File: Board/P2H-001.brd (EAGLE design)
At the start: 94.9 x 72.4 mm, 29 parts, among them IC1 74LS157N, IC2 LTC485N, IC3 74LS07N, IC4 LTC485N, IC5 4066N, IC6 TLC5941NT, IC7 TLC5941NT

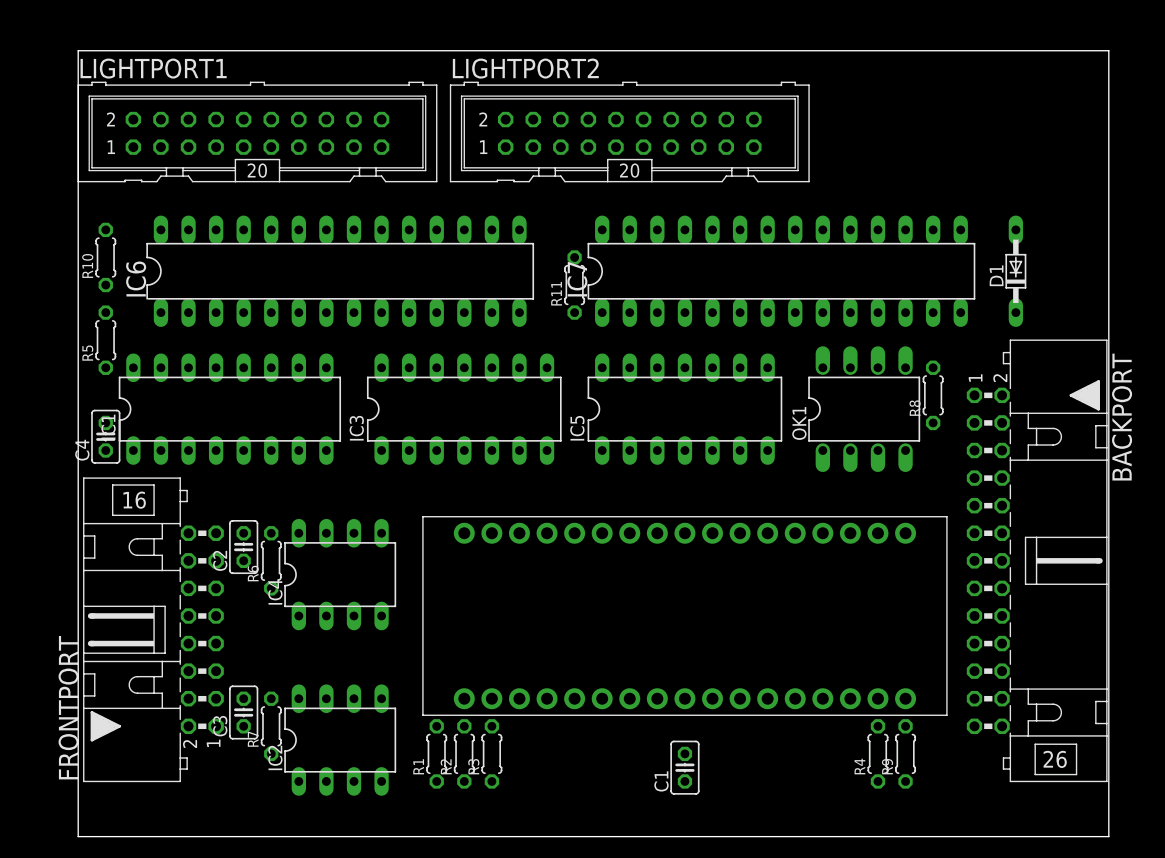
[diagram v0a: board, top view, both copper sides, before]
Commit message: Redesigned for ICB-93 size.
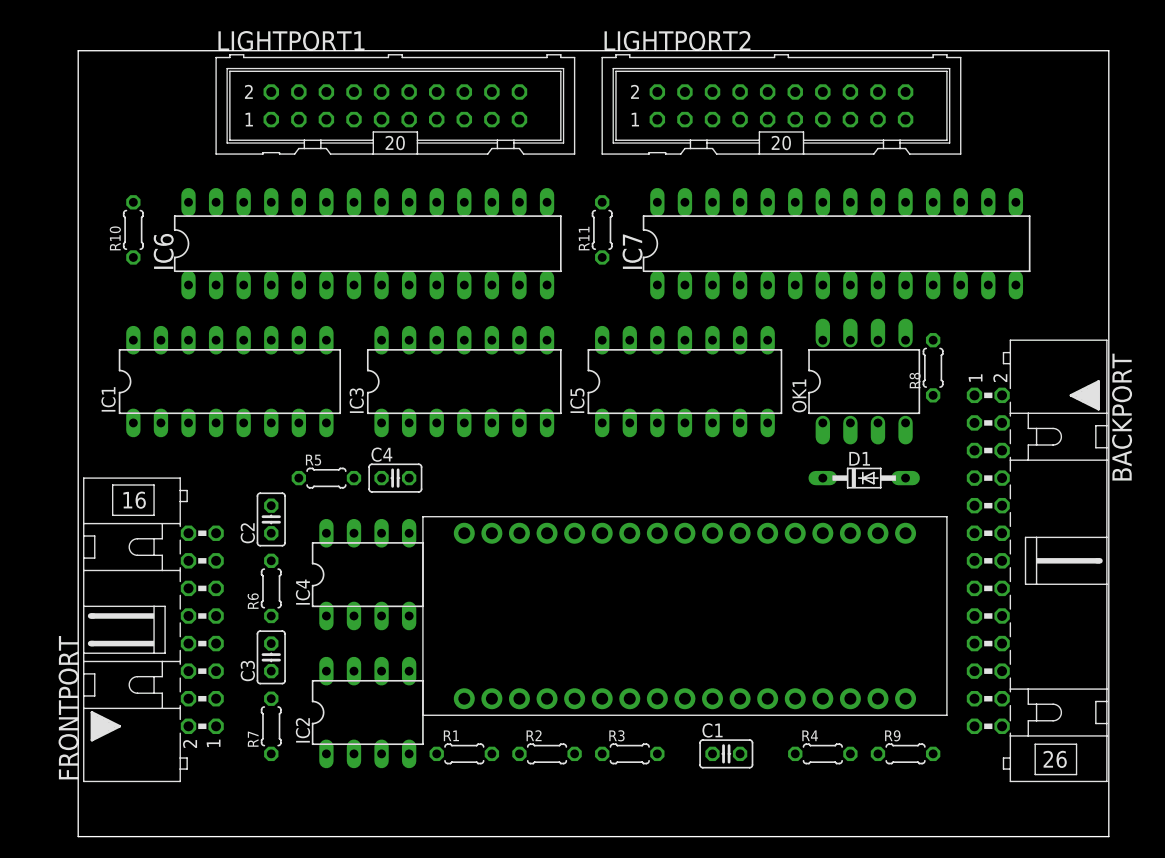
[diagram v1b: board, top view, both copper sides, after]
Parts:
- moved C4 26.9 mm to (29.2, 33.0), turned to 0 degrees
- moved R5 24.0 mm to (22.9, 33.0), turned to 0 degrees
- moved D1 23.6 mm to (72.4, 33.0), turned to 0 degrees
- moved LIGHTPORT2 14.2 mm to (64.8, 67.3)
- moved LIGHTPORT1 13.0 mm to (29.2, 67.3)
- moved R3 12.7 mm to (50.8, 7.62), turned to 0 degrees
- moved R2 7.62 mm to (43.2, 7.62), turned to 0 degrees
- moved R11 5.68 mm to (48.3, 55.9)
- moved C3 5.68 mm to (17.8, 16.5)
- moved IC7 5.68 mm to (69.8, 54.6)
- moved R4 5.08 mm to (68.6, 7.62), turned to 0 degrees
- moved C1 4.02 mm to (59.7, 7.62), turned to 0 degrees
- moved IC2 3.59 mm to (26.7, 11.4)
- moved IC6 3.59 mm to (26.7, 54.6)
- moved C2 3.59 mm to (17.8, 29.2)
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
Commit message: Design renewed.
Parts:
- removed IC7: TLC5941NT, adafruit:DIL28-3
- removed LIGHTPORT1, LIGHTPORT2: (no value), con-ml:ML20
- removed MC1: ARDUINOMICRO, adafruit:ARDUINOMICRO
- removed R10, R11: 4.7k, resistor:0204/5
- removed R9: 220, resistor:0204/5
- added C5, C6, C7: (no value), rcl:C025-025X050
- added JP1, JP2: (no value), pinhead:1X02
- added LIGHTPORT: (no value), con-ml:ML20L
- added U$1: ARDUINO_PRO_MINI, SparkFun-Boards:ARDUINO_PRO_MINI
- IC5: value 4066N -> TLC5941NT; device 40xx:DIL14 -> adafruit:DIL28-3
- R1, R2: value 330 -> 220
- R3: value 330 -> 120
- R4: value 220 -> 120
- R5: value 10k -> 220
- R6: value 120 -> 220
- R7: value 120 -> 4.7k
- R8: value 220 -> 4.7k
- moved IC2 66.7 mm to (69.8, 62.2)
- moved R3 56.8 mm to (61.0, 63.5), turned to 90 degrees
- moved R7 55.7 mm to (58.4, 48.3)
- moved IC1 51.8 mm to (64.8, 31.8)
- moved C2 51.1 mm to (59.7, 58.4), turned to 0 degrees
- moved C3 49.7 mm to (59.7, 43.2), turned to 0 degrees
- moved IC4 48.9 mm to (69.8, 47.0)
- moved R4 41.3 mm to (61.0, 48.3), turned to 90 degrees
- moved R6 35.7 mm to (53.3, 20.3)
- moved R5 35.4 mm to (55.9, 20.3), turned to 90 degrees
- moved OK1 29.7 mm to (44.5, 31.8)
- moved R8 28.7 mm to (58.4, 63.5)
- moved R1 28.4 mm to (61.0, 20.3), turned to 90 degrees
- moved D1 21.6 mm to (50.8, 31.8), turned to 90 degrees
- moved R2 19.8 mm to (58.4, 20.3), turned to 90 degrees
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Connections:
- removed net 3V3: FRONTPORT.3, MC1.P$33
- removed net GPDETECT: BACKPORT.8, MC1.P$7
- removed net LEDMAX: FRONTPORT.13, R1.1
- removed net LEDMIN: FRONTPORT.11, R3.1
- removed net N$44: IC7.5, LIGHTPORT2.10
- removed net N$45: IC7.7, LIGHTPORT2.12
- removed net N$46: IC7.9, LIGHTPORT2.14
- removed net N$47: IC7.11, LIGHTPORT2.16
- removed net N$48: IC7.13, LIGHTPORT2.18
- removed net N$49: IC7.15, LIGHTPORT2.20
- removed net N$50: IC7.2, LIGHTPORT2.7
- removed net N$51: IC7.4, LIGHTPORT2.9
- removed net N$52: IC7.6, LIGHTPORT2.11
- removed net N$53: IC7.8, LIGHTPORT2.13
- removed net N$54: IC7.10, LIGHTPORT2.15
- removed net N$55: IC7.12, LIGHTPORT2.17
- removed net N$56: IC7.14, LIGHTPORT2.19
- removed net N$57: IC6.28, LIGHTPORT1.5
- removed net N$65: IC6.15, LIGHTPORT1.20
- removed net N$66: IC6.2, LIGHTPORT1.7
- removed net N$67: IC6.4, LIGHTPORT1.9
- removed net N$68: IC6.6, LIGHTPORT1.11
- removed net N$69: IC6.8, LIGHTPORT1.13
- removed net N$70: IC6.10, LIGHTPORT1.15
- removed net N$71: IC6.12, LIGHTPORT1.17
- removed net N$72: IC6.14, LIGHTPORT1.19
- removed net N$73: IC6.11, LIGHTPORT1.16
- removed net N$74: IC6.7, LIGHTPORT1.12
- removed net N$75: IC6.9, LIGHTPORT1.14
- removed net N$76: IC6.5, LIGHTPORT1.10
- removed net N$77: IC6.3, LIGHTPORT1.8
- removed net N$78: IC6.1, LIGHTPORT1.6
- removed net N$80: IC6.13, LIGHTPORT1.18
- removed net SCL: BACKPORT.15, MC1.P$10
- removed net SDA: BACKPORT.14, MC1.P$11
- removed net VR: FRONTPORT.16, MC1.P$9
- removed net VSS: IC5.7
- removed net XDETECT: BACKPORT.10, IC1.1, MC1.P$1, R5.1
- new net LED1B: FRONTPORT.10, IC5.2
- new net LED1G: FRONTPORT.9, IC5.1
- new net LED1R: FRONTPORT.8, IC5.28
- new net LED2B: FRONTPORT.13, IC5.5
- new net LED2G: FRONTPORT.12, IC5.4
- new net LED2R: FRONTPORT.11, IC5.3
- new net LED3B: FRONTPORT.16, IC5.8
- new net LED3G: FRONTPORT.15, IC5.7
- new net LED3R: FRONTPORT.14, IC5.6
- new net N$17: BACKPORT.18, U$1.13
- new net N$20: BACKPORT.26, D1.A, OK1.3
- new net N$22: BACKPORT.17, IC5.13
- new net N$23: FRONTPORT.7, U$1.A4
- new net N$24: IC5.14, LIGHTPORT.3
- new net N$25: IC5.15, LIGHTPORT.4
- new net N$26: IC6.28, LIGHTPORT.5
- new net N$27: IC6.2, LIGHTPORT.7
- new net N$28: IC6.4, LIGHTPORT.9
- new net N$29: IC6.6, LIGHTPORT.11
- new net N$30: IC6.8, LIGHTPORT.13
- new net N$31: IC6.10, LIGHTPORT.15
- new net N$32: IC6.12, LIGHTPORT.17
- new net N$33: IC6.14, LIGHTPORT.19
- new net N$34: IC6.1, LIGHTPORT.6
- new net N$35: IC6.3, LIGHTPORT.8
- new net N$36: IC6.5, LIGHTPORT.10
- new net N$40: IC6.9, LIGHTPORT.14
- new net SWRST: FRONTPORT.4, U$1.3
- new net XBAR: BACKPORT.5, IC1.1, U$1.11
- net BLANK: now also BACKPORT.4, IC5.23, U$1.7; no longer IC5.2, IC7.23
- net GND: now also C5.2, C6.2, C7.2, IC1.10, IC1.11, IC1.13, IC1.14, IC1.5, IC1.6, IC3.11, IC3.13, IC3.3, IC3.5, IC3.9, IC5.22, LIGHTPORT.2, U$1.23; no longer BACKPORT.4, FRONTPORT.10, FRONTPORT.12, FRONTPORT.14, FRONTPORT.4, FRONTPORT.6, FRONTPORT.8, IC7.22, LIGHTPORT1.2, LIGHTPORT1.4, LIGHTPORT2.2, LIGHTPORT2.4, MC1.P$12, MC1.P$21
- net GSCLCK: now also IC5.18, U$1.8; no longer BACKPORT.12, IC7.18, MC1.P$8
- net HSRX: now also IC1.3; no longer IC1.2
- net MIDIRX: now also IC1.2, JP2.2; no longer IC1.3
- net MODE: now also IC5.27, U$1.9; no longer IC5.9, IC7.27
- net N$1: now also IC1.4, JP1.2, JP2.1; no longer BACKPORT.3, MC1.P$31
- net N$10: now also BACKPORT.10, U$1.20; no longer FRONTPORT.5, MC1.P$22
- net N$11: now also BACKPORT.13, IC5.9; no longer BACKPORT.11, IC5.4, MC1.P$27
- net N$12: now also BACKPORT.14, IC5.10; no longer BACKPORT.13, IC5.8, MC1.P$26
- net N$13: now also R5.1; no longer R8.1
- net N$14: now also BACKPORT.15, IC5.11; no longer BACKPORT.19, R9.1
- net N$15: now also BACKPORT.24, R2.2; no longer BACKPORT.20, R4.2
- net N$16: now also IC5.17, IC6.26; no longer IC6.17, IC7.26
- net N$18: now also BACKPORT.25, R5.2; no longer BACKPORT.21, R8.2
- net N$19: now also BACKPORT.11, U$1.A6; no longer BACKPORT.17, MC1.P$19
- net N$2: now also R2.1; no longer R4.1
- net N$21: now also BACKPORT.16, IC5.12; no longer MC1.P$3, R1.2
- net N$3: now also BACKPORT.6, U$1.12; no longer FRONTPORT.15, R2.1
- net N$37: now also IC5.20, R7.2; no longer IC6.20, R10.2
- net N$38: now also IC6.20, R8.2; no longer IC7.20, R11.2
- net N$39: now also IC6.7, LIGHTPORT.12; no longer IC7.28, LIGHTPORT2.5
- net N$4: now also BACKPORT.23, R6.1; no longer BACKPORT.5, MC1.P$30
- net N$41: now also IC6.11, LIGHTPORT.16; no longer IC7.1, LIGHTPORT2.6
- net N$42: now also IC6.13, LIGHTPORT.18; no longer BACKPORT.22, D1.A, OK1.3
- net N$43: now also IC6.15, LIGHTPORT.20; no longer IC7.3, LIGHTPORT2.8
- net N$5: now also BACKPORT.12, U$1.A7; no longer MC1.P$4, R3.2
- net N$6: now also U$1.17; no longer MC1.P$29
- net N$7: now also FRONTPORT.3, R1.1; no longer MC1.P$34, R2.2
- net N$8: now also BACKPORT.8, U$1.18; no longer IC5.13, IC5.5, IC5.6, MC1.P$2
- net N$9: now also U$1.19; no longer IC5.1, MC1.P$28
- net RX: now also JP1.1, U$1.2; no longer IC1.4, MC1.P$14
- net RX+: now also BACKPORT.19, R4.1; no longer BACKPORT.23, R7.1
- net RX-: now also BACKPORT.20, R4.2; no longer BACKPORT.24, R7.2
- net SCLCK: now also IC5.25, U$1.16; no longer BACKPORT.18, IC7.25, MC1.P$18
- net SIN: now also IC5.26, U$1.14; no longer BACKPORT.16, IC6.26, MC1.P$17
- net SWMAX: now also FRONTPORT.6, U$1.6; no longer FRONTPORT.9, MC1.P$5
- net SWMIN: now also FRONTPORT.5, U$1.5; no longer FRONTPORT.7, MC1.P$6
- net TX: now also U$1.1; no longer MC1.P$15
- net TX+: now also BACKPORT.21, R3.1; no longer BACKPORT.25, R6.1
- net TX-: now also BACKPORT.22, R3.2; no longer BACKPORT.26, R6.2
- net VCC: now also BACKPORT.1, C5.1, C6.1, C7.1, IC5.19, IC5.21, R6.2, R7.1, R8.1, U$1.21; no longer BACKPORT.6, IC7.19, IC7.21, MC1.P$23, R10.1, R11.1, R5.2, R9.2
- net VDD: now also BACKPORT.3, LIGHTPORT.1, R1.2, U$1.24; no longer BACKPORT.1, IC5.14, LIGHTPORT1.1, LIGHTPORT1.3, LIGHTPORT2.1, LIGHTPORT2.3, MC1.P$20
- net XLAT: now also IC5.24, U$1.10; no longer IC5.3, IC7.24

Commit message: Slightly re-arranged.
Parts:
- moved BACKPORT 10.2 mm to (82.5, 35.6)
- moved D1 2.54 mm to (53.3, 31.8)
- moved IC1 2.54 mm to (67.3, 31.8)
- moved IC2 2.54 mm to (72.4, 62.2)
- moved IC4 2.54 mm to (72.4, 47.0)
- moved C4 2.54 mm to (17.8, 47.0)
- moved C5 2.54 mm to (17.8, 62.2)
- moved C6 2.54 mm to (17.8, 31.8)
- moved C1 2.54 mm to (62.2, 7.62)
- moved C2 2.54 mm to (62.2, 58.4)
- moved C3 2.54 mm to (62.2, 43.2)
- moved C7 2.54 mm to (62.2, 15.2)
- moved IC3 2.54 mm to (30.5, 31.8)
- moved IC5 2.54 mm to (39.4, 47.0)
- moved IC6 2.54 mm to (39.4, 62.2)
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
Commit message: Autorouted.
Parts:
- renumbered BACKPORT to SV2, FRONTPORT to SV1, LIGHTPORT to SV3
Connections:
- net N$3 renamed GDETECT
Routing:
- net GND: track 0.00 -> 400.2 mm
- net VCC: track 0.00 -> 310.3 mm, vias 0 -> 5
- net N$8: track 0.00 -> 170.4 mm
- net BLANK: track 0.00 -> 168.5 mm, vias 0 -> 4
- net VDD: track 0.00 -> 154.4 mm, vias 0 -> 5
- net TX: track 0.00 -> 141.3 mm
- net XBAR: track 0.00 -> 122.7 mm
- net MODE: track 0.00 -> 103.7 mm, vias 0 -> 3
- net N$25: track 0.00 -> 97.6 mm, vias 0 -> 1
- net N$30: track 0.00 -> 94.8 mm, vias 0 -> 2
- net XLAT: track 0.00 -> 87.3 mm, vias 0 -> 5
- net SWRST: track 0.00 -> 86.0 mm, vias 0 -> 1
- net GSCLCK: track 0.00 -> 84.6 mm, vias 0 -> 2
- net N$9: track 0.00 -> 83.0 mm, vias 0 -> 2
- net TX+: track 0.00 -> 74.3 mm
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
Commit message: square design.
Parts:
- removed JP2: (no value), pinhead:1X02
- moved C1 54.6 mm to (62.2, 62.2), turned to 90 degrees
- moved C2 25.7 mm to (36.8, 54.6)
- moved C3 25.7 mm to (36.8, 39.4)
- moved IC1 25.4 mm to (41.9, 31.8)
- moved JP1 22.9 mm to (54.6, 31.8)
- moved SV2 19.0 mm to (63.5, 35.6)
- moved IC2 17.8 mm to (54.6, 62.2)
- moved IC4 17.8 mm to (54.6, 47.0)
- moved R7 16.6 mm to (47.0, 39.4), turned to 0 degrees
- moved R8 16.6 mm to (47.0, 54.6), turned to 0 degrees
- moved C4 13.7 mm to (29.2, 39.4), turned to 0 degrees
- moved C5 13.7 mm to (29.2, 54.6), turned to 0 degrees
- moved OK1 13.7 mm to (52.1, 19.1)
- moved R1 13.1 mm to (57.1, 8.89)
- moved R2 13.1 mm to (54.6, 8.89)
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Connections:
- net MIDIRX: no longer JP2.2
- net N$1: no longer JP2.1
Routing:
- net GND: track 400.2 -> 265.3 mm
- net N$8: track 170.4 -> 54.1 mm, vias 0 -> 2
- net SWRST: track 86.0 -> 18.6 mm, vias 1 -> 0
- net VCC: track 310.3 -> 252.1 mm, vias 5 -> 2
- net N$30: track 94.8 -> 51.6 mm, vias 2 -> 3
- net XLAT: track 87.3 -> 122.1 mm, vias 5 -> 3
- net N$17: track 59.0 -> 25.7 mm, vias 2 -> 1
- net TX: track 141.3 -> 108.4 mm, vias 0 -> 4
- net VDD: track 154.4 -> 182.7 mm, vias 5 -> 1
- net XBAR: track 122.7 -> 94.9 mm, vias 0 -> 2
- net TX-: track 56.9 -> 80.8 mm
- net TX+: track 74.3 -> 52.1 mm
- net N$40: track 56.7 -> 36.8 mm
- net BLANK: track 168.5 -> 149.2 mm, vias 4 -> 2
- net N$18: track 34.0 -> 14.7 mm
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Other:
- board size 94.9 x 72.4 mm -> 72.1 x 72.4 mm

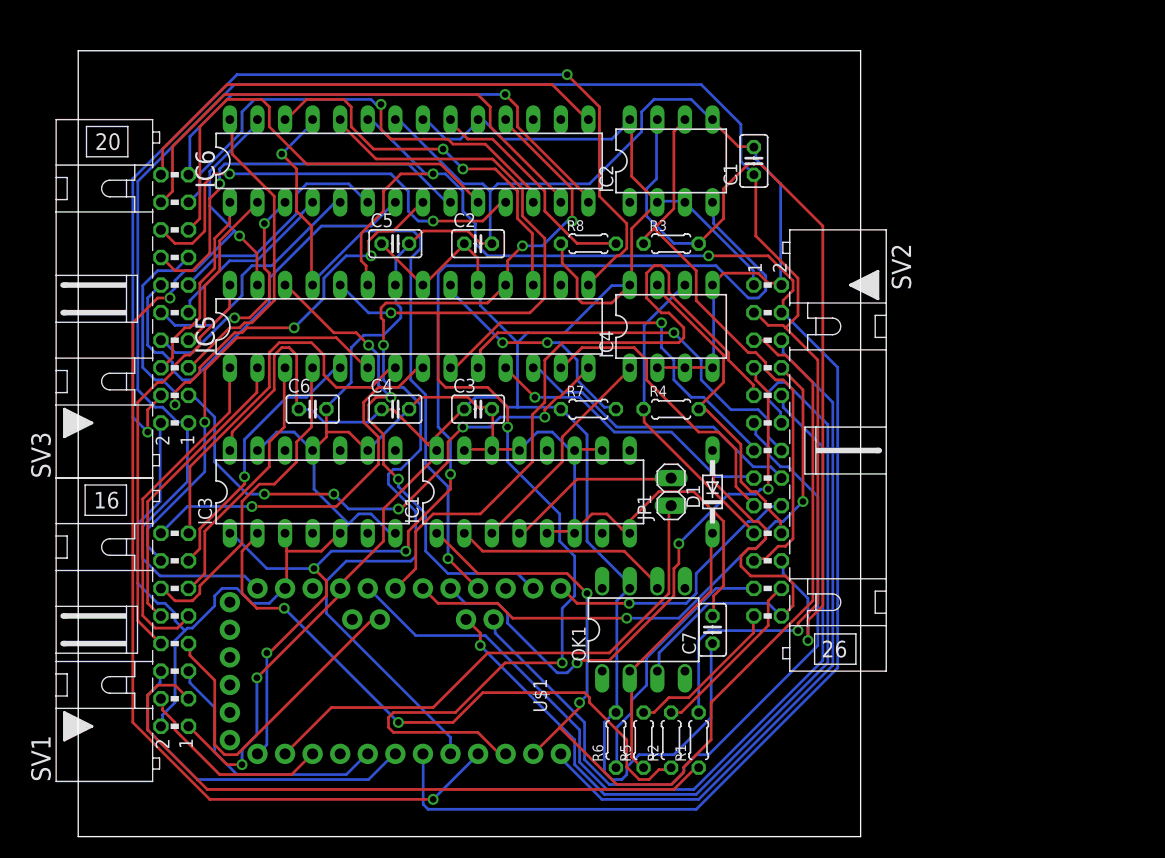
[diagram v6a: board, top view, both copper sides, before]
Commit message: Routed by 0.10mm paths.
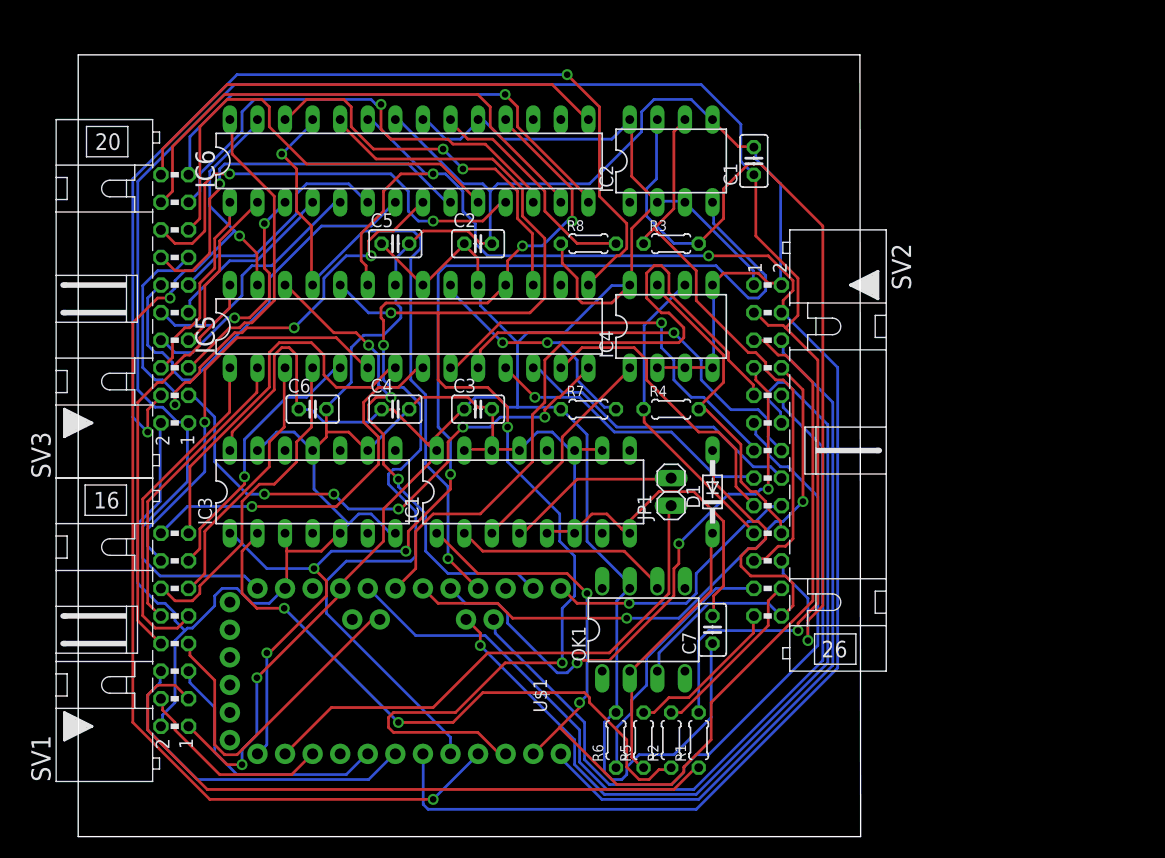
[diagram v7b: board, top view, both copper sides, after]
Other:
- board size 72.1 x 72.4 mm -> 72.1 x 72 mm
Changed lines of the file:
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@@
 <plain>
 <wire x1="0" y1="0" x2="72.06" y2="0" width="0" layer="20"/>
-<wire x1="72.06" y1="0" x2="72.06" y2="72.38" width="0" layer="20"/>
-<wire x1="72.06" y1="72.38" x2="0" y2="72.38" width="0" layer="20"/>
-<wire x1="0" y1="72.38" x2="0" y2="0" width="0" layer="20"/>
-<dimension x1="0" y1="0" x2="0" y2="72.39" x3="-7.62" y3="36.195" textsize="1.778" layer="20"/>
-<dimension x1="0" y1="0" x2="72.39" y2="0" x3="36.195" y3="-2.54" textsize="1.778" layer="20"/>
+<wire x1="72.06" y1="0" x2="72" y2="72" width="0" layer="20"/>
+<wire x1="72" y1="72" x2="0" y2="72" width="0" layer="20"/>
+<wire x1="0" y1="72" x2="0" y2="0" width="0" layer="20"/>
+<dimension x1="0" y1="0" x2="0" y2="72" x3="-5.08" y3="36" textsize="1.778" layer="20"/>
+<dimension x1="0" y1="0" x2="72.06" y2="0" x3="36.03" y3="-2.54" textsize="1.778" layer="20"/>
 </plain>
 <attributes>

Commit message: slightly optimized.
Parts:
- moved C2 10.2 mm to (47.0, 54.6)
- moved C3 10.2 mm to (47.0, 39.4)
- moved R7 8.89 mm to (38.1, 39.4)
- moved R8 8.89 mm to (38.1, 54.6)
- moved C6 2.54 mm to (19.1, 39.4)
- moved R3 1.27 mm to (55.9, 54.6)
- moved R4 1.27 mm to (55.9, 39.4)
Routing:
- net VCC: track 252.1 -> 323.9 mm
- net GND: track 265.3 -> 313.4 mm, vias 0 -> 2
- net N$25: track 95.0 -> 50.3 mm, vias 2 -> 1
- net N$2: track 57.4 -> 97.5 mm
- net GSCLCK: track 91.6 -> 129.5 mm, vias 3 -> 2
- net N$30: track 51.6 -> 23.7 mm, vias 3 -> 2
- net TX-: track 80.8 -> 53.4 mm
- net N$19: track 67.8 -> 42.1 mm
- net N$10: track 82.2 -> 59.1 mm, vias 0 -> 1
- net LED1R: track 38.0 -> 58.3 mm
- net N$33: track 47.3 -> 66.6 mm, vias 1 -> 0
- net N$9: track 67.8 -> 48.7 mm, vias 0 -> 1
- net TX: track 108.4 -> 89.6 mm, vias 4 -> 5
- net VDD: track 182.7 -> 163.9 mm, vias 1 -> 3
- net TX+: track 52.1 -> 69.6 mm, vias 0 -> 1
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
